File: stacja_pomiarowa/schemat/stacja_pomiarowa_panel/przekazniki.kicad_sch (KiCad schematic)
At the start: 96 parts, among them J1 Conn_01x02, J10 Conn_01x02, J11 Conn_01x02, J12 Conn_01x02, J13 Conn_01x02, J14 Conn_01x02, J15 Conn_01x02, J16 Conn_01x02, J2 Conn_01x02, J3 Conn_01x02, J4 Conn_01x02, J5 Conn_01x02, J6 Conn_01x02, J7 Conn_01x02, J8 Conn_01x02, J9 Conn_01x02, K5 FINDER-36.11, Q1 BC547, Q10 BC547, Q11 BC547, Q12 BC547, Q13 BC547, Q14 BC547, Q15 BC547, Q16 BC547, Q2 BC547, Q3 BC547, Q4 BC547, Q5 BC547, Q6 BC547, Q7 BC547, Q8 BC547, Q9 BC547

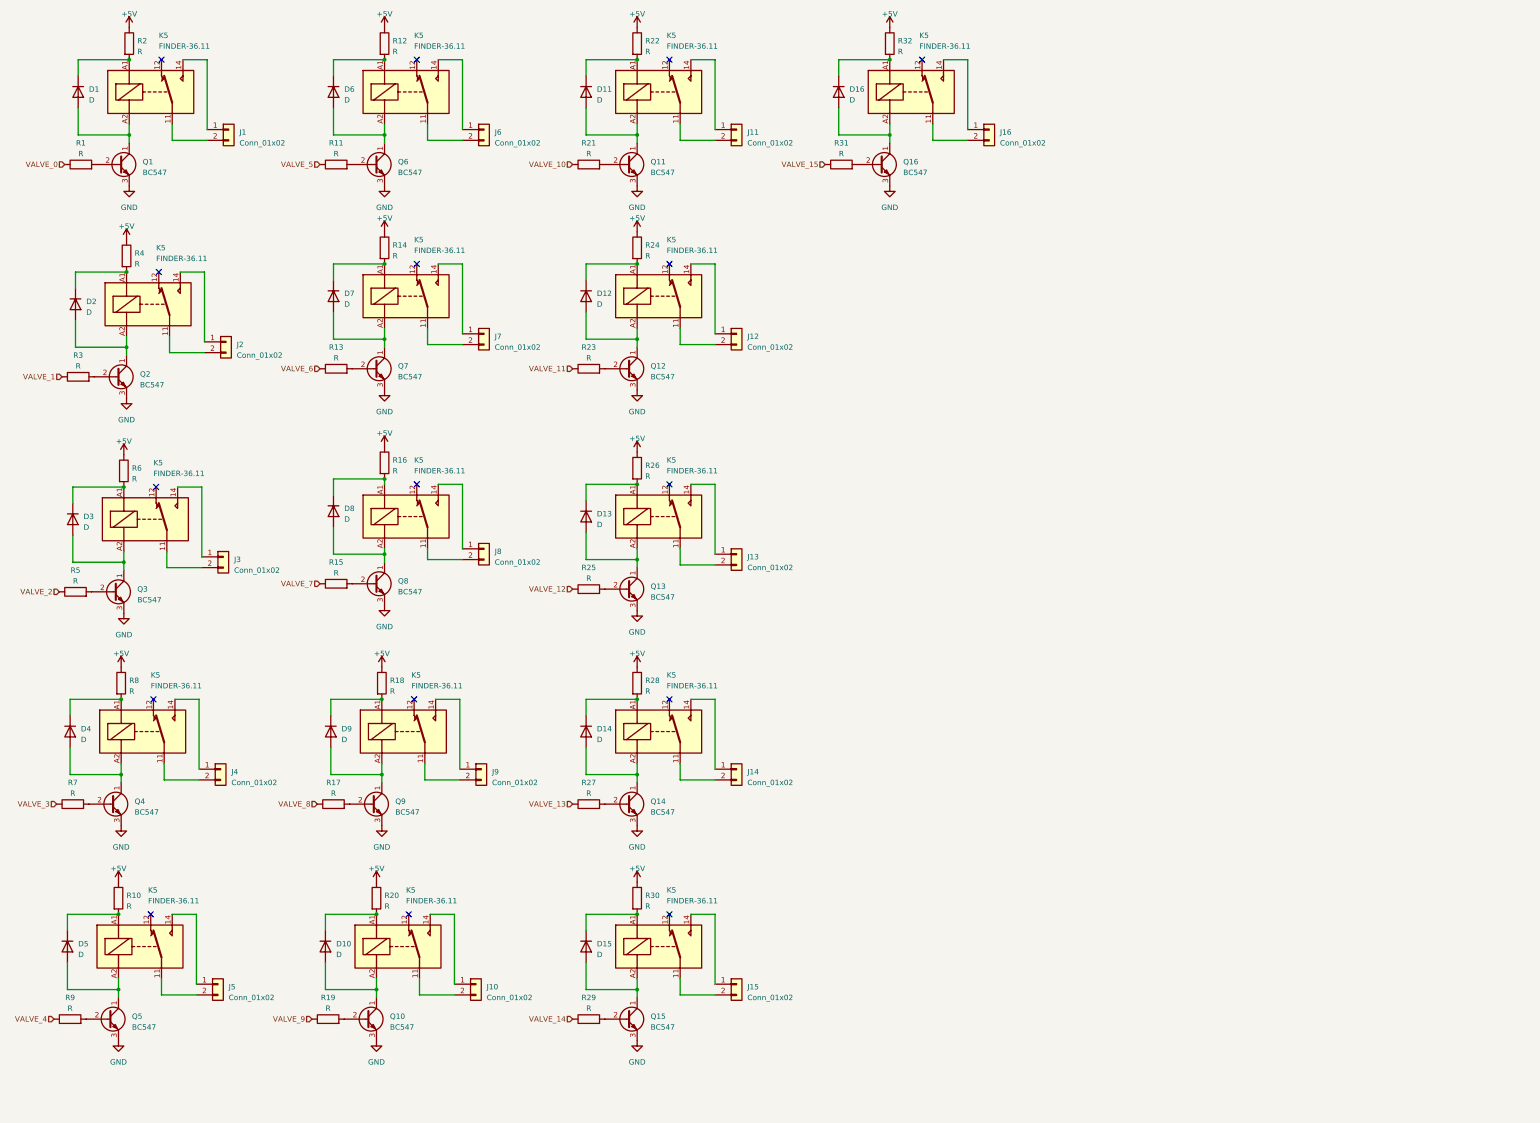
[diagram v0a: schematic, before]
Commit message: Dodano do fragmentu schematu z przekaźnikami zewnętrzne źródło zasilania AC
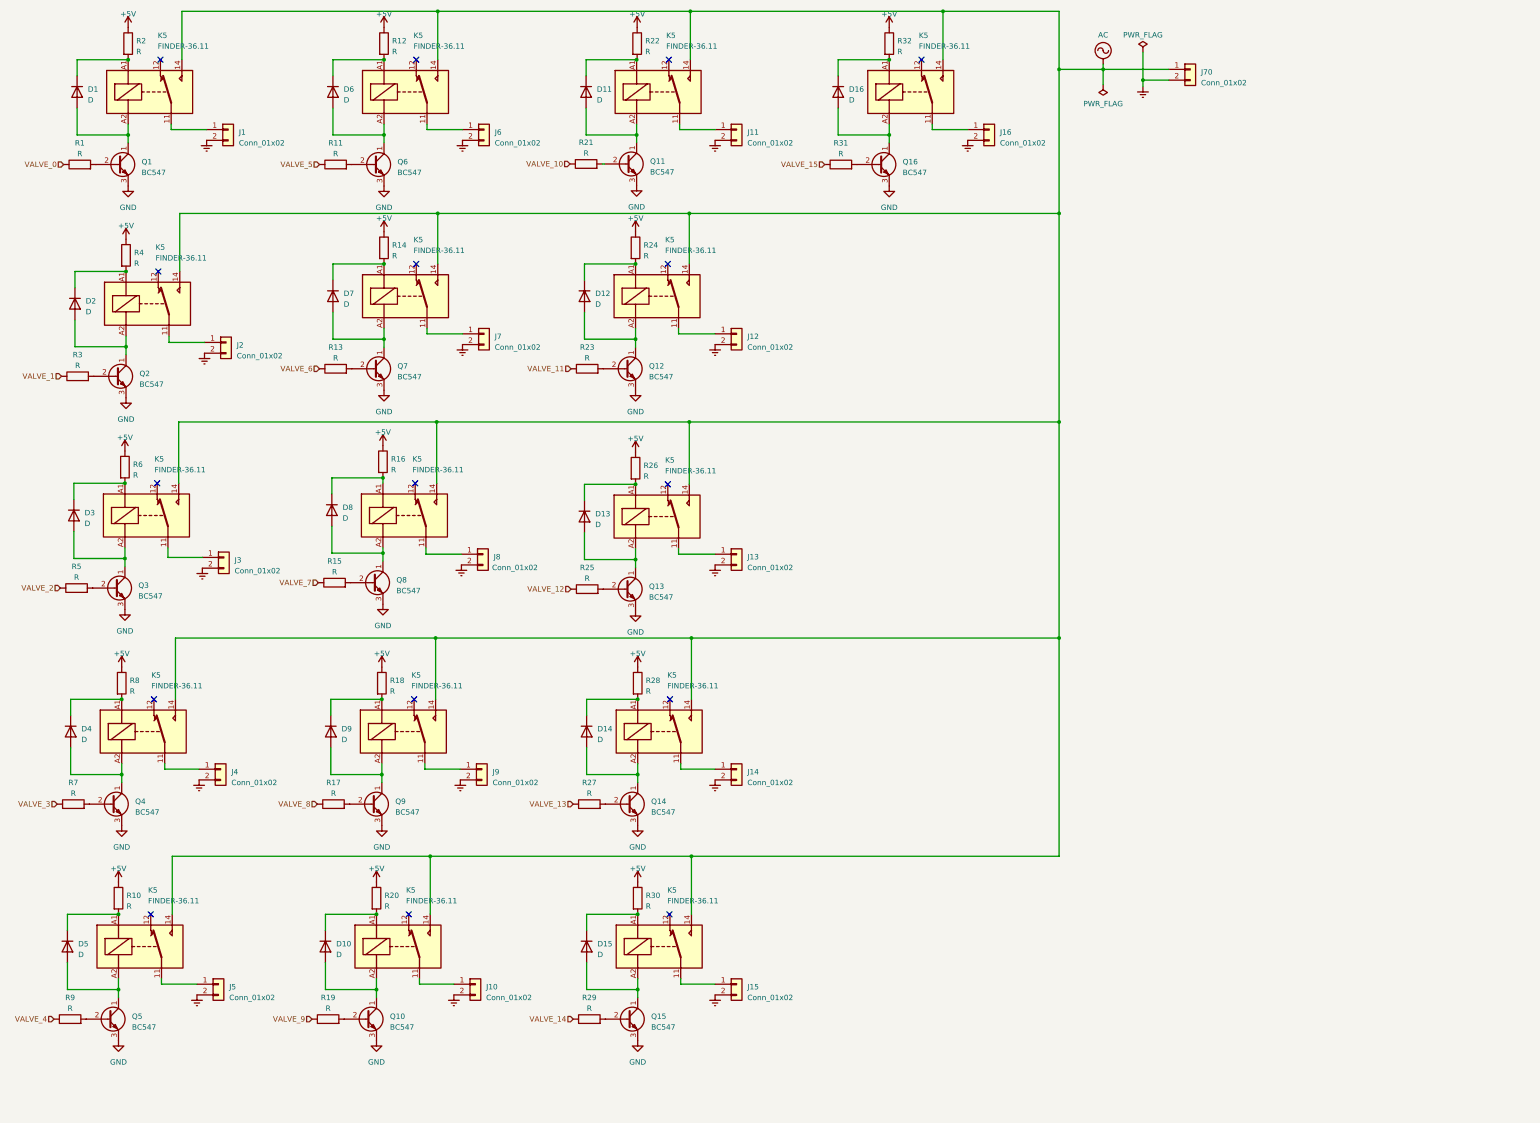
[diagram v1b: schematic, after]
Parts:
- added J70: Conn_01x02, symbol Connector_Generic:Conn_01x02
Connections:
- net at J4.1 (Pin_1): now also K5.11; no longer K5.14
- net Earth: now reaches J4.2 (Pin_2)
- net Earth: now also J1.2 (Pin_2), J10.2 (Pin_2), J11.2 (Pin_2), J12.2 (Pin_2), J13.2 (Pin_2), J14.2 (Pin_2), J15.2 (Pin_2), J16.2 (Pin_2), J2.2 (Pin_2), J3.2 (Pin_2), J5.2 (Pin_2), J6.2 (Pin_2), J7.2 (Pin_2), J8.2 (Pin_2), J9.2 (Pin_2), J70.2 (Pin_2); no longer K5.11
- net at J2.1 (Pin_1): now also K5.11; no longer K5.14
- net at K5.11: now also J16.1 (Pin_1); no longer J16.2 (Pin_2)
- net AC: now reaches K5.14
- net AC: now also K5.14, K5.14, K5.14, K5.14, K5.14, K5.14, K5.14, K5.14, K5.14, K5.14, K5.14, K5.14, K5.14, K5.14, K5.14, J70.1 (Pin_1); no longer J16.1 (Pin_1)
- net at K5.11: now also J10.1 (Pin_1); no longer J10.2 (Pin_2)
- net at K5.11: now also J1.1 (Pin_1); no longer J1.2 (Pin_2)
- net at J13.1 (Pin_1): now also K5.11; no longer K5.14
- net at K5.11: now also J14.1 (Pin_1); no longer J14.2 (Pin_2)
- net at K5.11: now also J5.1 (Pin_1); no longer J5.2 (Pin_2)
- net at J8.1 (Pin_1): now also K5.11; no longer K5.14
- net at J12.1 (Pin_1): now also K5.11; no longer K5.14
- net at J7.1 (Pin_1): now also K5.11; no longer K5.14
- net at K5.11: now also J6.1 (Pin_1); no longer J6.2 (Pin_2)
- net at K5.11: now also J11.1 (Pin_1); no longer J11.2 (Pin_2)
- net at J3.1 (Pin_1): now also K5.11; no longer K5.14
- net at K5.11: now also J9.1 (Pin_1); no longer J9.2 (Pin_2)
- net at J15.1 (Pin_1): now also K5.11; no longer K5.14
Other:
- moved on the sheet: D3, J8, K5, Q3, R21, R5, R6

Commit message: Dodano ledy informujące czy urządzenie połączyło się z systemem, dodane tytuły podschematów ze złączami
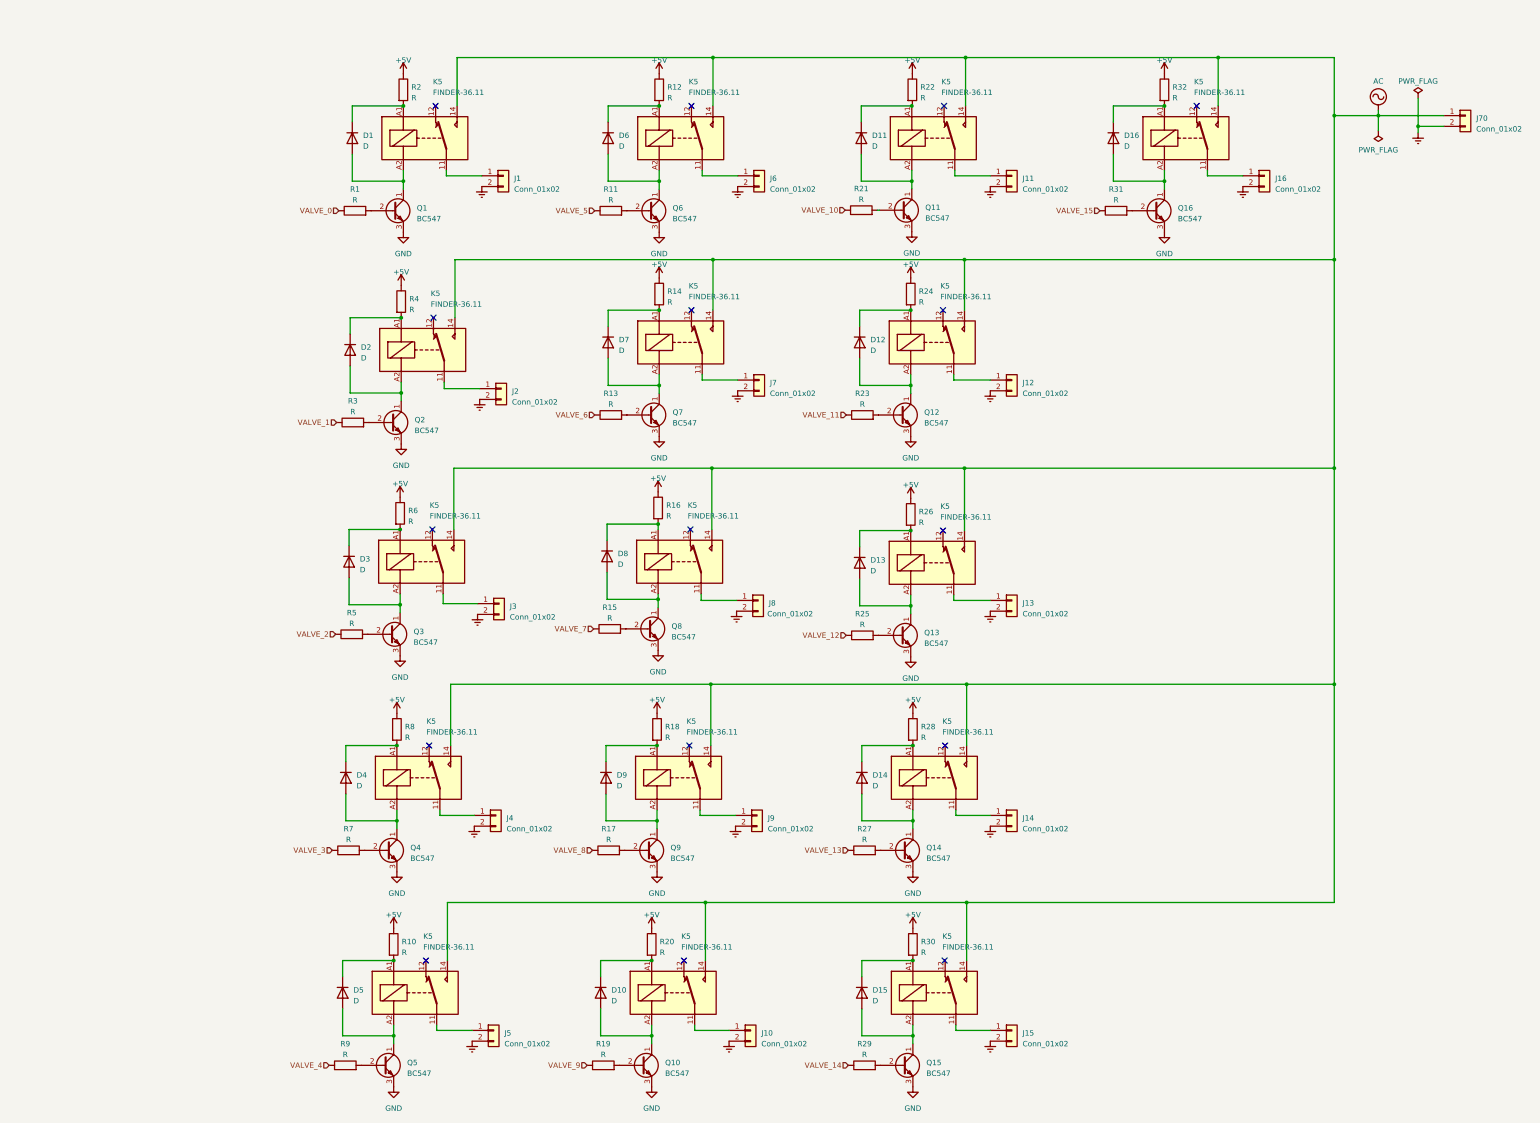
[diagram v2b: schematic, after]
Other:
- title: (none) -> Złącza z przekaźnikami
- moved on the sheet: D1, D10, D11, D12, D13, D14, D15, D16, D2, D3, D4, D5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
